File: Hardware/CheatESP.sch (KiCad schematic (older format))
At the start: 10 parts, among them SW1 SW_Push, SW2 SW_Push, SW3 SW_Push, SW4 SW_Push

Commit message: Finished the init string cleanup
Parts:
- SW1: value SW_Push -> Interface_Switch_1
- SW2: value SW_Push -> Flash_Switch
- SW3: value SW_Push -> Interface_Switch_2
- SW4: value SW_Push -> Reset_Button
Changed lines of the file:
@@
 P 3650 4500
 F 0 "SW2" V 3750 4550 50  0000 L CNN
-F 1 "SW_Push" H 3650 4440 50  0000 C CNN
+F 1 "Flash_Switch" H 3650 4440 50  0000 C CNN
 F 2 "" H 3650 4700 50  0001 C CNN
 F 3 "" H 3650 4700 50  0001 C CNN
@@
 P 5450 4200
 F 0 "SW4" V 5500 4300 50  0000 L CNN
-F 1 "SW_Push" H 5450 4140 50  0000 C CNN
+F 1 "Reset_Button" V 5350 4450 50  0000 C CNN
 F 2 "" H 5450 4400 50  0001 C CNN
 F 3 "" H 5450 4400 50  0001 C CNN
@@
 P 3550 3700
 F 0 "SW1" H 3600 3850 50  0000 L CNN
-F 1 "SW_Push" H 3550 3640 50  0000 C CNN
+F 1 "Interface_Switch_1" H 3550 3640 50  0000 C CNN
 F 2 "" H 3550 3900 50  0001 C CNN
 F 3 "" H 3550 3900 50  0001 C CNN
@@
 P 5050 4300
 F 0 "SW3" H 5100 4400 50  0000 L CNN
-F 1 "SW_Push" H 5050 4240 50  0000 C CNN
+F 1 "Interface_Switch_2" H 4900 4200 50  0000 C CNN
 F 2 "" H 5050 4500 50  0001 C CNN
 F 3 "" H 5050 4500 50  0001 C CNN

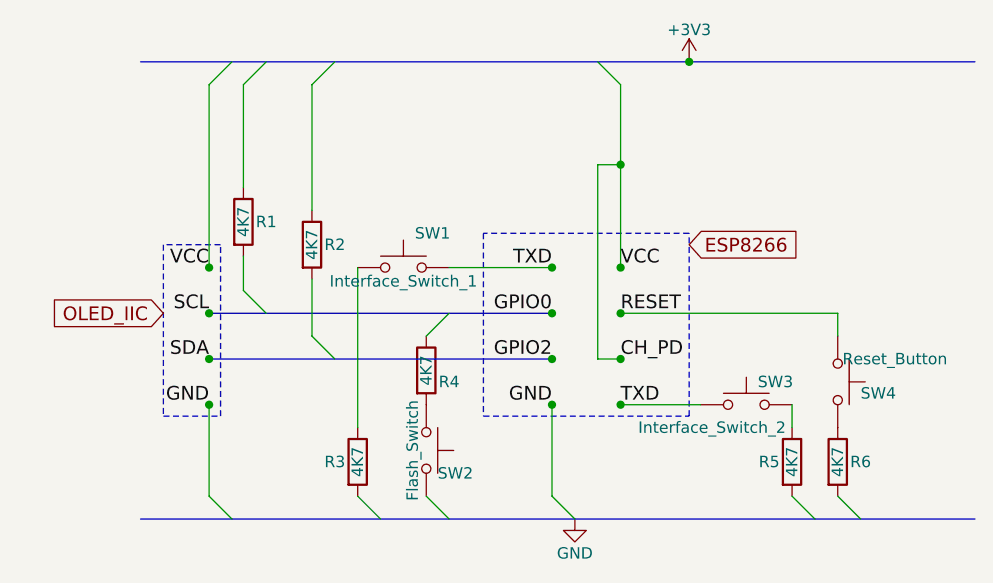
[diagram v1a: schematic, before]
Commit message: Added code to interface the button on U0RXD. TODO create a test server to extensively test the OLED driving functions
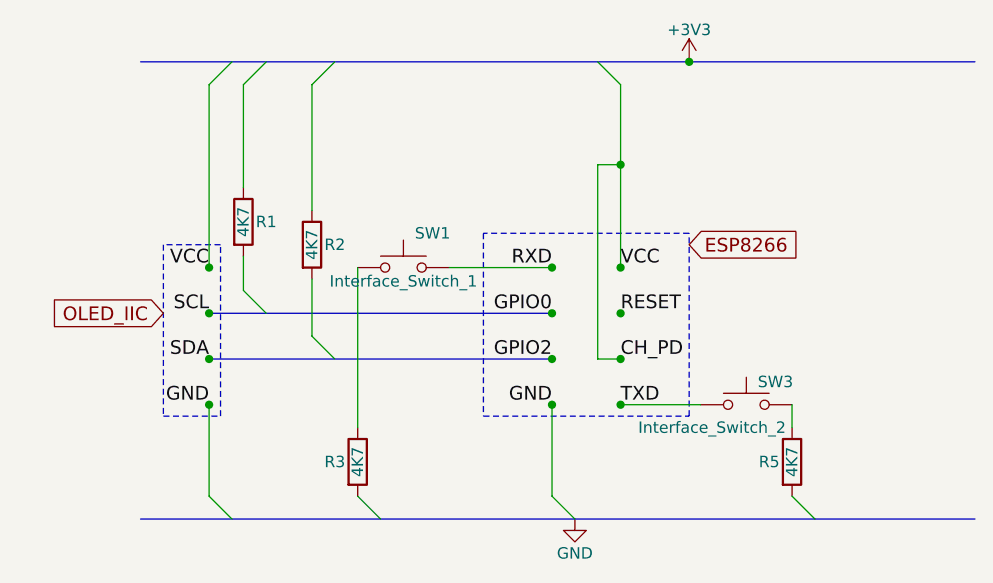
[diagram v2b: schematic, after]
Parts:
- removed R4, R6: 4K7, symbol R
- removed SW2: Flash_Switch, symbol SW_Push
- removed SW4: Reset_Button, symbol SW_Push
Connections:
- net TXD: no longer SW1.2
- new net RXD: SW1.2
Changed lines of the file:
@@
 TXD
 Text Label 4200 3700 2    60   ~ 0
-TXD
+RXD
 Text Label 4200 3900 2    60   ~ 0
 GPIO0
@@
 OLED_IIC
 Entry Wire Line
-	5450 4700 5550 4800
-$Comp
-L SW_Push SW2
-U 1 1 5AFC44C9
-P 3650 4500
-F 0 "SW2" V 3750 4550 50  0000 L CNN
-F 1 "Flash_Switch" H 3650 4440 50  0000 C CNN
-F 2 "" H 3650 4700 50  0001 C CNN
-F 3 "" H 3650 4700 50  0001 C CNN
-	1    3650 4500
-	0    1    1    0
-$EndComp
-$Comp
-L R R6
-U 1 1 5AFC4539
-P 5450 4550
-F 0 "R6" H 5550 4550 50  0000 C CNN
-F 1 "4K7" V 5450 4550 50  0000 C CNN
-F 2 "" V 5380 4550 50  0001 C CNN
-F 3 "" H 5450 4550 50  0001 C CNN
-	1    5450 4550
-	1    0    0    -1
-$EndComp
-$Comp
-L SW_Push SW4
-U 1 1 5AFC46EA
-P 5450 4200
-F 0 "SW4" V 5500 4300 50  0000 L CNN
-F 1 "Reset_Button" V 5350 4450 50  0000 C CNN
-F 2 "" H 5450 4400 50  0001 C CNN
-F 3 "" H 5450 4400 50  0001 C CNN
-	1    5450 4200
-	0    1    1    0
-$EndComp
-Wire Wire Line
-	4500 3900 5450 3900
-Wire Wire Line
-	5450 3900 5450 4000
-Entry Wire Line
-	3650 4700 3750 4800
-Entry Wire Line
-	3650 4000 3750 3900
-$Comp
-L R R4
-U 1 1 5AFC49A3
-P 3650 4150
-F 0 "R4" H 3750 4100 50  0000 C CNN
-F 1 "4K7" V 3650 4150 50  0000 C CNN
-F 2 "" V 3580 4150 50  0001 C CNN
-F 3 "" H 3650 4150 50  0001 C CNN
-	1    3650 4150
-	1    0    0    -1
-$EndComp
-Entry Wire Line
 	2850 3800 2950 3900

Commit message: Updated the circuit.
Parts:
- removed R5: 4K7, symbol R
- removed SW3: Interface_Switch_2, symbol SW_Push
- added R4, R5, R6, R7: 4K7, symbol CheatESP-rescue:R
- added SW2: Flash Button, symbol CheatESP-rescue:SW_Push
- added SW3: RST Button, symbol CheatESP-rescue:SW_Push
- R1, R2, R3: symbol R -> CheatESP-rescue:R
- SW1: value Interface_Switch_1 -> Interface button; symbol SW_Push -> CheatESP-rescue:SW_Push
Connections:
- net CH_PD: now also R7.2
- net RESET: now also R5.1, SW3.1
- new net: R4.1, SW2.1
- new net: R6.1, SW3.2
- new net VCC: R7.1
- no-connect marks 0 -> 1
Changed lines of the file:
@@
-EESchema Schematic File Version 2
-LIBS:power
-LIBS:device
-LIBS:switches
-LIBS:relays
-LIBS:motors
-LIBS:transistors
-LIBS:conn
-LIBS:linear
-LIBS:regul
-LIBS:74xx
-LIBS:cmos4000
-LIBS:adc-dac
-LIBS:memory
-LIBS:xilinx
-LIBS:microcontrollers
-LIBS:dsp
-LIBS:microchip
-LIBS:analog_switches
-LIBS:motorola
-LIBS:texas
-LIBS:intel
-LIBS:audio
-LIBS:interface
-LIBS:digital-audio
-LIBS:philips
-LIBS:display
-LIBS:cypress
-LIBS:siliconi
-LIBS:opto
-LIBS:atmel
-LIBS:contrib
-LIBS:valves
+EESchema Schematic File Version 4
 LIBS:CheatESP-cache
-EELAYER 25 0
+EELAYER 26 0
 EELAYER END
 $Descr A4 11693 8268
@@
 $EndDescr
 $Comp
-L GND #PWR?
+L power:GND #PWR01
 U 1 1 5AFC39E3
 P 4300 4800
-F 0 "#PWR?" H 4300 4550 50  0001 C CNN
+F 0 "#PWR01" H 4300 4550 50  0001 C CNN
 F 1 "GND" H 4300 4650 50  0000 C CNN
 F 2 "" H 4300 4800 50  0001 C CNN
@@
 $EndComp
 $Comp
-L +3V3 #PWR?
+L power:+3V3 #PWR02
 U 1 1 5AFC39F7
 P 4800 2800
-F 0 "#PWR?" H 4800 2650 50  0001 C CNN
+F 0 "#PWR02" H 4800 2650 50  0001 C CNN
 F 1 "+3V3" H 4800 2940 50  0000 C CNN
 F 2 "" H 4800 2800 50  0001 C CNN
@@
 Entry Wire Line
 	4200 4700 4300 4800
-Entry Wire Line
-	4400 2800 4500 2900
-$Comp
-L R R1
+$Comp
+L CheatESP-rescue:R R1
 U 1 1 5AFC3E5D
 P 2850 3500
@@
 $EndComp
 $Comp
-L R R2
+L CheatESP-rescue:R R2
 U 1 1 5AFC3F5A
 P 3150 3600
@@
 	1    0    0    -1
 $EndComp
-Connection ~ 4500 3700
-Connection ~ 4500 3900
-Connection ~ 4500 4100
-Connection ~ 4500 4300
-Connection ~ 4200 4300
-Connection ~ 4200 4100
-Connection ~ 4200 3900
-Connection ~ 4200 3700
-Connection ~ 4800 2800
-Connection ~ 2700 3900
-Connection ~ 2700 4100
-Connection ~ 2700 4300
-Connection ~ 2700 3700
-Wire Bus Line
-	2400 4800 6050 4800
-Wire Wire Line
-	4500 2900 4500 3700
-Wire Wire Line
-	4500 4100 4400 4100
-Wire Wire Line
-	4400 4100 4400 3250
-Wire Wire Line
-	4400 3250 4500 3250
-Connection ~ 4500 3250
-Wire Bus Line
-	2700 3900 4200 3900
-Wire Bus Line
-	2700 4100 4200 4100
 Wire Wire Line
 	4200 4300 4200 4700
@@
 Wire Notes Line
 	4800 3550 3900 3550
-Text GLabel 4800 3600 2    60   Input ~ 0
+Text GLabel 4350 4150 1    60   Input ~ 0
 ESP8266
 Wire Notes Line
@@
 Wire Wire Line
 	2850 3800 2850 3650
-Wire Bus Line
-	2400 2800 6050 2800
 Entry Wire Line
 	3150 2900 3250 2800
@@
 	3150 2900 3150 3450
 $Comp
-L R R3
+L CheatESP-rescue:R R3
 U 1 1 5AFED44E
 P 3350 4550
@@
 $EndComp
 $Comp
-L R R5
-U 1 1 5AFED49B
-P 5250 4550
-F 0 "R5" H 5150 4550 50  0000 C CNN
-F 1 "4K7" V 5250 4550 50  0000 C CNN
-F 2 "" V 5180 4550 50  0001 C CNN
-F 3 "" H 5250 4550 50  0001 C CNN
-	1    5250 4550
-	1    0    0    -1
-$EndComp
-$Comp
-L SW_Push SW1
+L CheatESP-rescue:SW_Push SW1
 U 1 1 5AFED4DA
 P 3550 3700
 F 0 "SW1" H 3600 3850 50  0000 L CNN
-F 1 "Interface_Switch_1" H 3550 3640 50  0000 C CNN
+F 1 "Interface button" H 3550 3640 50  0000 C CNN
 F 2 "" H 3550 3900 50  0001 C CNN
 F 3 "" H 3550 3900 50  0001 C CNN
@@
 	1    0    0    -1
 $EndComp
-$Comp
-L SW_Push SW3
-U 1 1 5AFED68F
-P 5050 4300
-F 0 "SW3" H 5100 4400 50  0000 L CNN
-F 1 "Interface_Switch_2" H 4900 4200 50  0000 C CNN
-F 2 "" H 5050 4500 50  0001 C CNN
-F 3 "" H 5050 4500 50  0001 C CNN
-	1    5050 4300
-	1    0    0    -1
-$EndComp
-Entry Wire Line
-	5250 4700 5350 4800
 Entry Wire Line
 	3350 4700 3450 4800
@@
 	3750 3700 4200 3700
 Wire Wire Line
-	5250 4300 5250 4400
-Wire Wire Line
 	4850 4300 4500 4300
+Entry Wire Line
+	3700 3900 3800 4000
+$Comp
+L CheatESP-rescue:SW_Push SW2
+U 1 1 5B73B57D
+P 3800 4350
+F 0 "SW2" H 3850 4500 50  0000 L CNN
+F 1 "Flash Button" H 3800 4600 50  0000 C CNN
+F 2 "" H 3800 4550 50  0001 C CNN
+F 3 "" H 3800 4550 50  0001 C CNN
+	1    3800 4350
+	0    -1   -1   0
+$EndComp
+Entry Wire Line
+	4100 4700 4200 4800
+NoConn ~ 4850 4300
+$Comp
+L CheatESP-rescue:SW_Push SW3
+U 1 1 5B73C7B5
+P 5700 4100
+F 0 "SW3" H 5750 4250 50  0000 L CNN
+F 1 "RST Button" H 5700 4040 50  0000 C CNN
+F 2 "" H 5700 4300 50  0001 C CNN
+F 3 "" H 5700 4300 50  0001 C CNN
+	1    5700 4100
+	0    1    1    0
+$EndComp
+$Comp
+L CheatESP-rescue:R R5
+U 1 1 5B73C818
+P 5700 3350
+F 0 "R5" H 5800 3350 50  0000 C CNN
+F 1 "4K7" V 5700 3350 50  0000 C CNN
+F 2 "" V 5630 3350 50  0001 C CNN
+F 3 "" H 5700 3350 50  0001 C CNN
+	1    5700 3350
+	1    0    0    1
+$EndComp
+Entry Wire Line
+	5700 4700 5800 4800
+Entry Wire Line
+	5600 2800 5700 2900
+Wire Wire Line
+	5700 2900 5700 3200
+Wire Wire Line
+	5700 3500 5700 3900
+Connection ~ 5700 3900
+Wire Wire Line
+	4500 3900 5700 3900
+Entry Wire Line
+	4950 2800 5050 2900
+Wire Wire Line
+	5050 2900 5050 3700
+Wire Wire Line
+	5050 4100 4500 4100
+Wire Wire Line
+	4500 3700 5050 3700
+$Comp
+L CheatESP-rescue:R R4
+U 1 1 5B73EFFF
+P 3950 4550
+F 0 "R4" H 3850 4500 50  0000 C CNN
+F 1 "4K7" V 3950 4550 50  0000 C CNN
+F 2 "" V 3880 4550 50  0001 C CNN
+F 3 "" H 3950 4550 50  0001 C CNN
+	1    3950 4550
+	0    -1   -1   0
+$EndComp
+Wire Wire Line
+	4100 4700 4100 4550
+Wire Wire Line
+	3800 4150 3800 4000
+$Comp
+L CheatESP-rescue:R R6
+U 1 1 5B73F718
+P 5700 4500
+F 0 "R6" H 5600 4450 50  0000 C CNN
+F 1 "4K7" V 5700 4500 50  0000 C CNN
+F 2 "" V 5630 4500 50  0001 C CNN
+F 3 "" H 5700 4500 50  0001 C CNN
+	1    5700 4500
+	1    0    0    -1
+$EndComp
+Wire Wire Line
+	5700 4350 5700 4300
+Wire Wire Line
+	5700 4650 5700 4700
+$Comp
+L CheatESP-rescue:R R7
+U 1 1 5B73FEFA
+P 5050 3900
+F 0 "R7" H 4950 3850 50  0000 C CNN
+F 1 "4K7" V 5050 3900 50  0000 C CNN
+F 2 "" V 4980 3900 50  0001 C CNN
+F 3 "" H 5050 3900 50  0001 C CNN
+	1    5050 3900
+	1    0    0    -1
+$EndComp
+Wire Wire Line
+	5050 3750 5050 3700
+Connection ~ 5050 3700
+Wire Wire Line
+	5050 4050 5050 4100
+Wire Bus Line
+	2700 4100 4200 4100
+Wire Bus Line
+	2700 3900 4200 3900
+Wire Bus Line
+	2400 4800 6050 4800
+Wire Bus Line
+	2400 2800 6050 2800
 $EndSCHEMATC
